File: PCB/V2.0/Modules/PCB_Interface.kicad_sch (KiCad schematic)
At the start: 8 parts, among them J10 Right_Connector, J11 Right_Connector, J12 Right_Connector, J17 Conn_02x04_Odd_Even, J18 Conn_02x04_Odd_Even, J3 Conn_02x04_Odd_Even, J8 Right_Connector, J9 Right_Connector

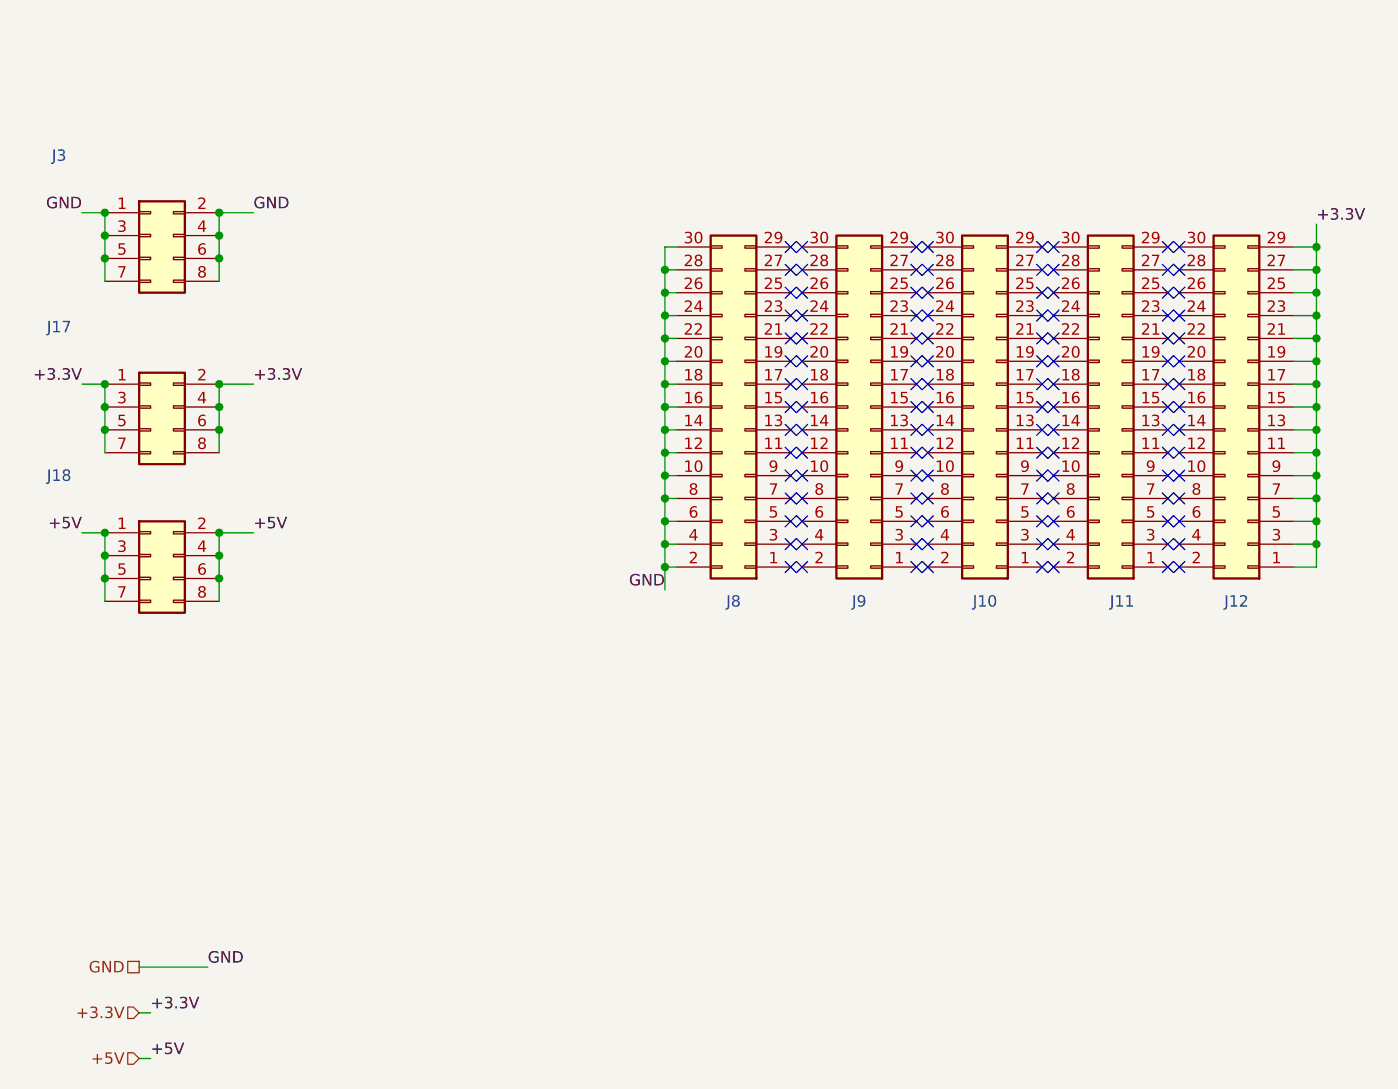
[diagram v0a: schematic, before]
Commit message: Update V2.0 form factor
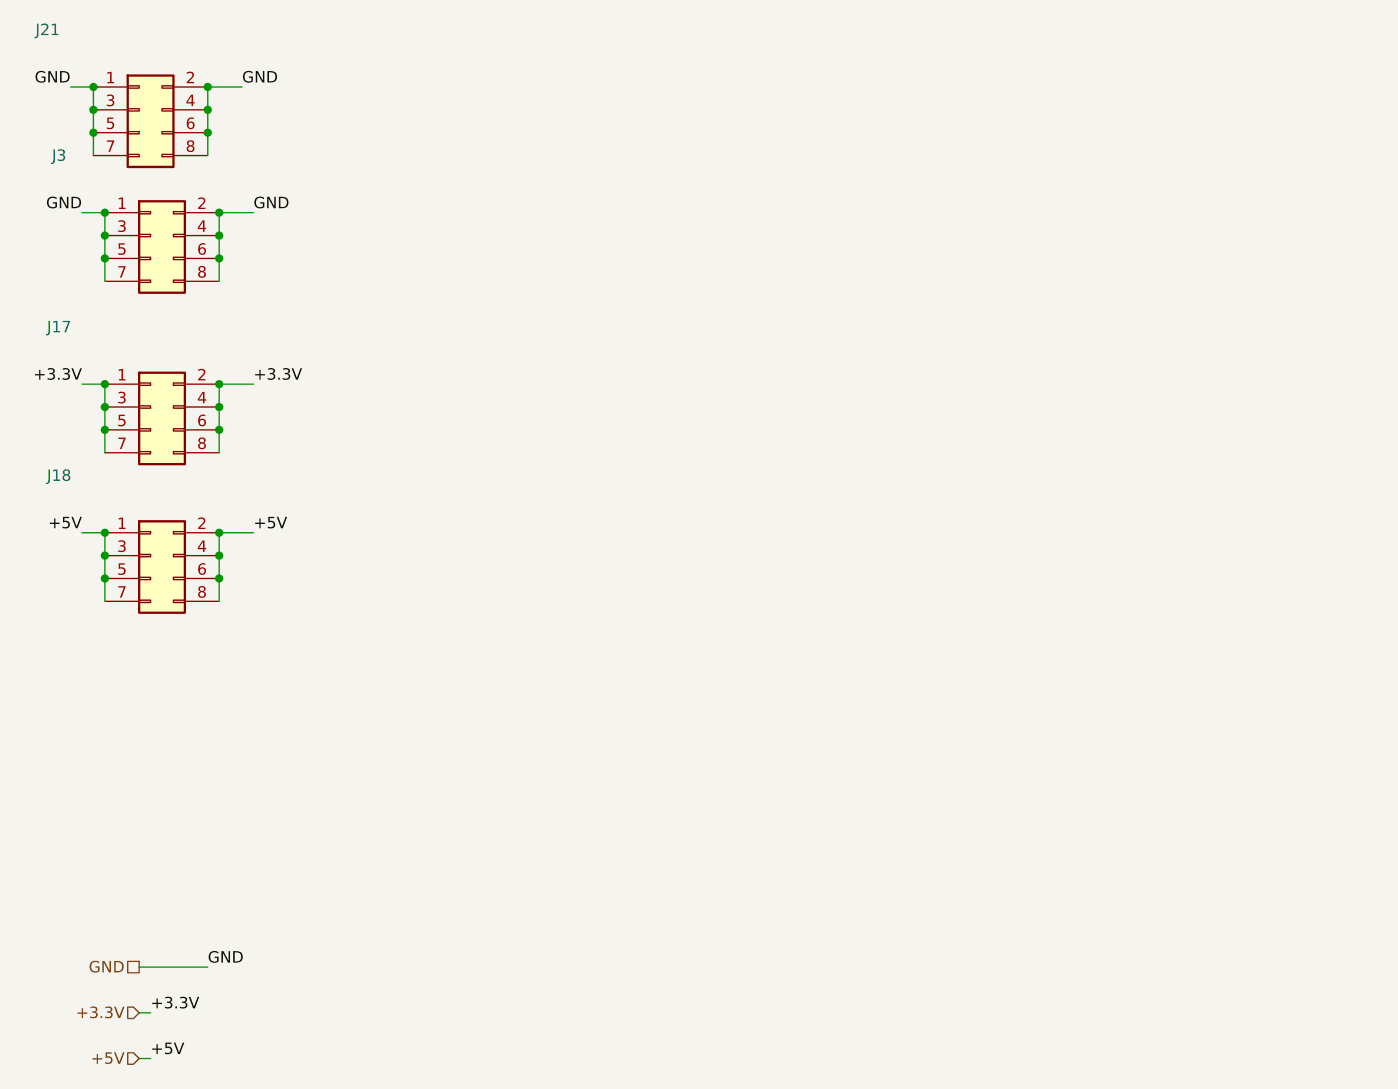
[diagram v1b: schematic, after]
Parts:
- removed J10, J11, J12, J8, J9: Right_Connector, Connector_PinHeader_2.54mm:PinHeader_2x15_P2.54mm_Vertical, symbol Connector_Generic:Conn_02x15_Odd_Even
- added J21: Conn_02x04_Odd_Even, Connector_PinHeader_2.54mm:PinHeader_2x04_P2.54mm_Vertical, symbol Connector_Generic:Conn_02x04_Odd_Even
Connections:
- net GND: now also J21.1 (Pin_1), J21.2 (Pin_2), J21.3 (Pin_3), J21.4 (Pin_4), J21.5 (Pin_5), J21.6 (Pin_6), J21.7 (Pin_7), J21.8 (Pin_8)
- no-connect marks 120 -> 0
